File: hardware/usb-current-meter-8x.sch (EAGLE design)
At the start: 154 parts, among them IC10 OPA2234U, IC12 LTC485S, IC2 OPA2234U, IC3 MEGA48/88/168-AU, IC4 OPA2234U, IC5 OPA2234U, IC6 OPA2234U, IC7 OPA2234U, IC8 OPA2234U, IC9 OPA2234U, U3 RJ45-8PTH, X1 MC2, X2 MC2, X3 MC2, X4 MC2, X5 MC2, X6 MC2, X7 MC2, X8 MC2

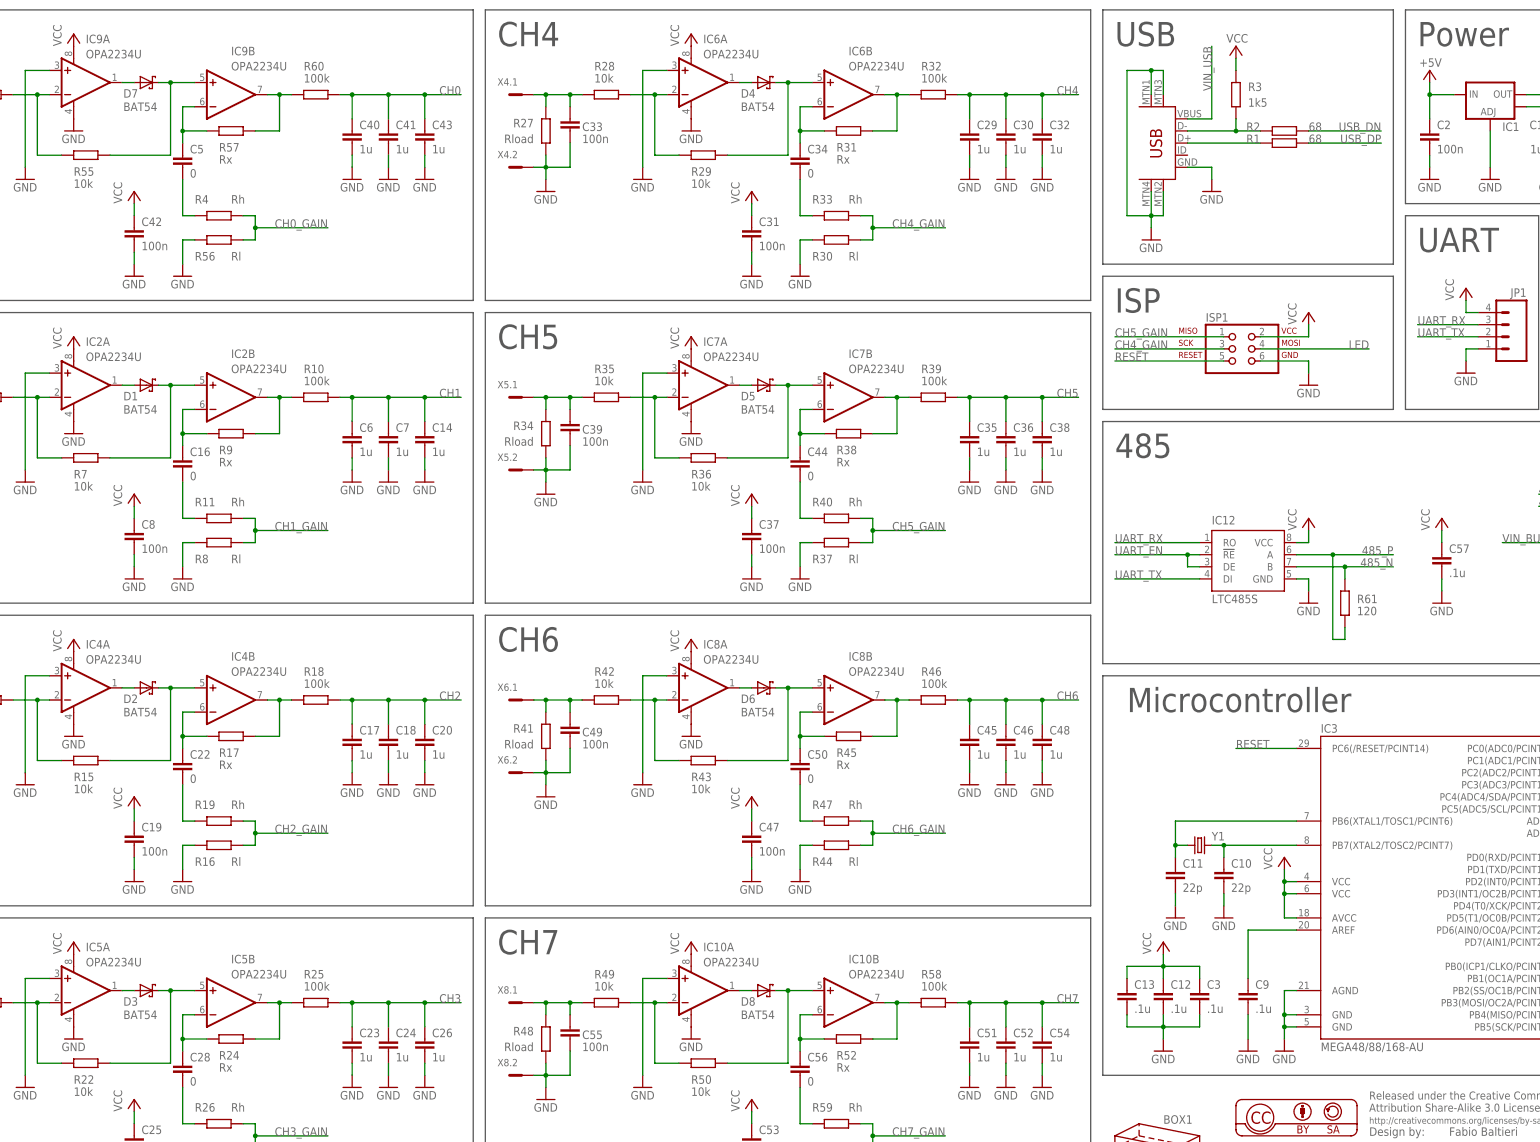
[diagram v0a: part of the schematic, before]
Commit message: hw: 8x: add part numbers
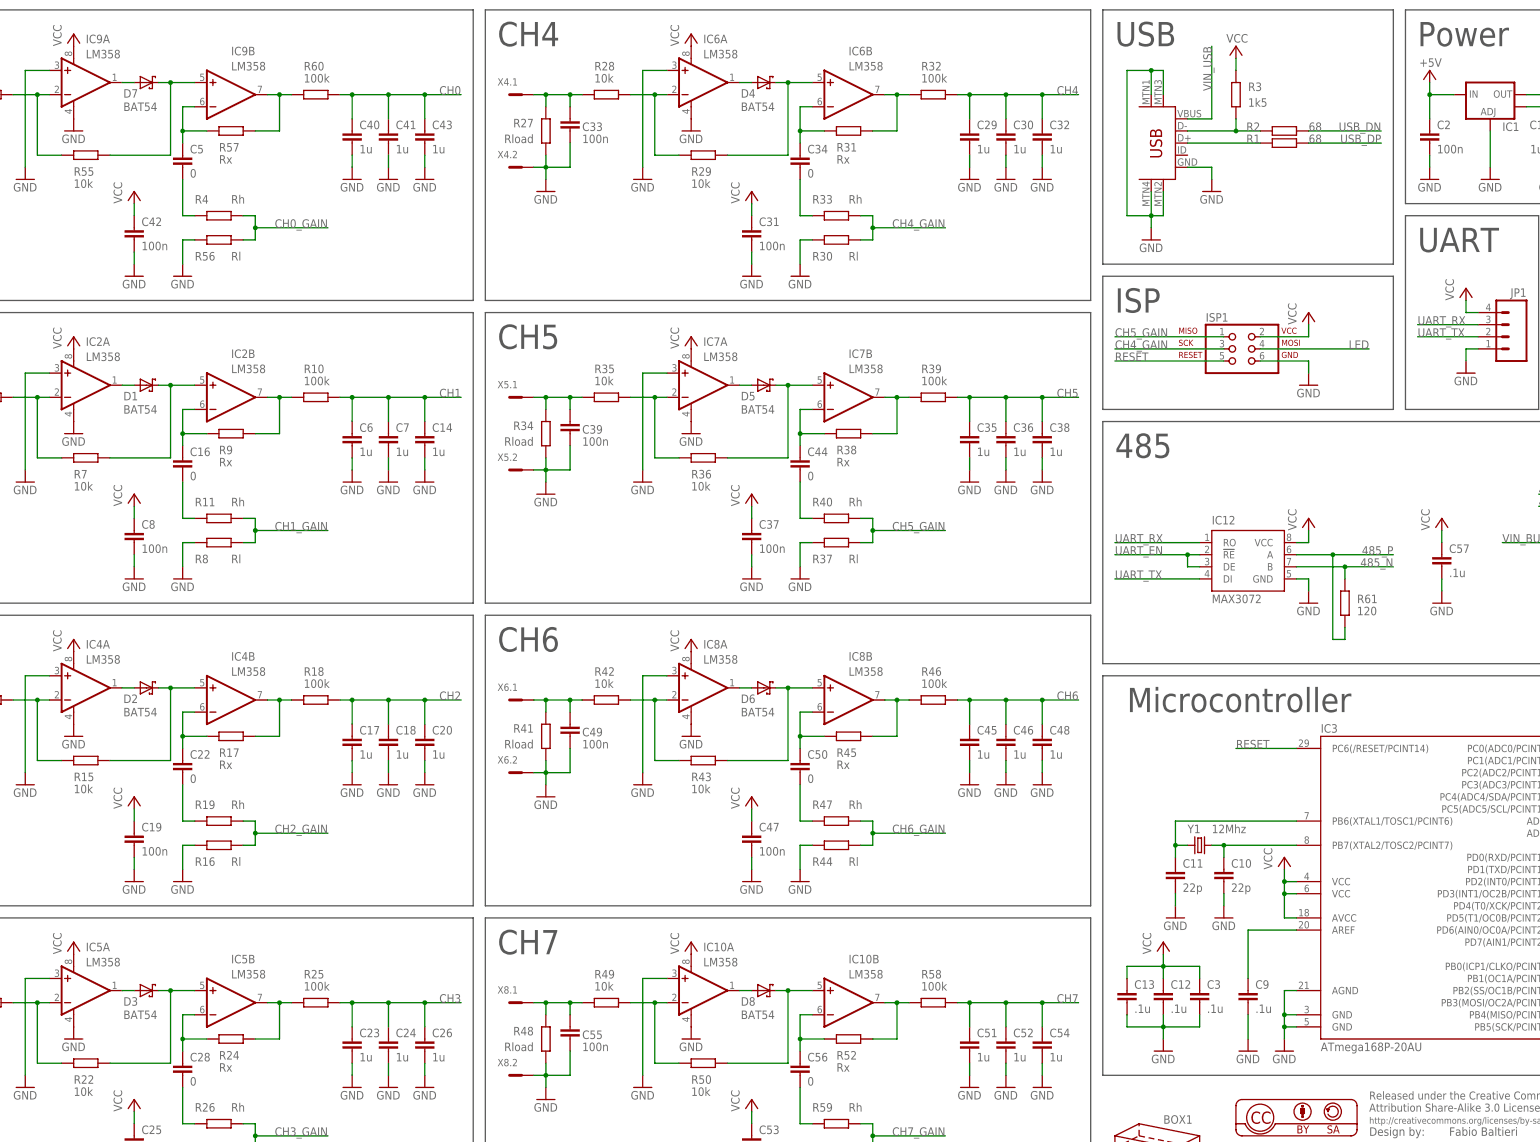
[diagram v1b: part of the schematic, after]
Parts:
- IC10, IC2, IC4, IC5, IC6, IC7, IC8, IC9: value OPA2234U -> LM358
- IC12: value LTC485S -> MAX3072
- IC3: value MEGA48/88/168-AU -> ATmega168P-20AU
- Y1: value (none) -> 12Mhz
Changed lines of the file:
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@@
 <part name="U$1" library="SparkFun" deviceset="USB-MINIB" device="-5PIN"/>
 <part name="GND11" library="supply1" deviceset="GND" device=""/>
-<part name="Y1" library="SparkFun" deviceset="CRYSTAL" device="HC49UV"/>
+<part name="Y1" library="SparkFun" deviceset="CRYSTAL" device="HC49UV" value="12Mhz"/>
 <part name="P+10" library="supply1" deviceset="VCC" device=""/>
 <part name="C9" library="rcl" deviceset="C-EU" device="C0805" value=".1u"/>
@@
 <part name="C12" library="rcl" deviceset="C-EU" device="C0805" value=".1u"/>
 <part name="C13" library="rcl" deviceset="C-EU" device="C0805" value=".1u"/>
-<part name="IC3" library="avr-5" deviceset="MEGA48/88/168" device="-AU"/>
+<part name="IC3" library="avr-5" deviceset="MEGA48/88/168" device="-AU" value="ATmega168P-20AU"/>
 <part name="FRAME1" library="frames" deviceset="DINA3_L" device=""/>
-<part name="IC9" library="burr-brown" deviceset="OPA2234" device="U"/>
+<part name="IC9" library="burr-brown" deviceset="OPA2234" device="U" value="LM358"/>
 <part name="X7" library="con-phoenix-381_l" deviceset="MC2" device=""/>
 <part name="D7" library="diode" deviceset="BAT54" device=""/>
@@
 <part name="P+6" library="supply1" deviceset="VCC" device=""/>
 <part name="GND7" library="supply1" deviceset="GND" device=""/>
-<part name="IC2" library="burr-brown" deviceset="OPA2234" device="U"/>
+<part name="IC2" library="burr-brown" deviceset="OPA2234" device="U" value="LM358"/>
 <part name="X1" library="con-phoenix-381_l" deviceset="MC2" device=""/>
 <part name="D1" library="diode" deviceset="BAT54" device=""/>
@@
 <part name="R11" library="rcl" deviceset="R-EU_" device="R0603" value="Rh"/>
 <part name="C16" library="rcl" deviceset="C-EU" device="C0805" value="0"/>
-<part name="IC4" library="burr-brown" deviceset="OPA2234" device="U"/>
+<part name="IC4" library="burr-brown" deviceset="OPA2234" device="U" value="LM358"/>
 <part name="X2" library="con-phoenix-381_l" deviceset="MC2" device=""/>
 <part name="D2" library="diode" deviceset="BAT54" device=""/>
@@
 <part name="R19" library="rcl" deviceset="R-EU_" device="R0603" value="Rh"/>
 <part name="C22" library="rcl" deviceset="C-EU" device="C0805" value="0"/>
-<part name="IC5" library="burr-brown" deviceset="OPA2234" device="U"/>
+<part name="IC5" library="burr-brown" deviceset="OPA2234" device="U" value="LM358"/>
 <part name="X3" library="con-phoenix-381_l" deviceset="MC2" device=""/>
 <part name="D3" library="diode" deviceset="BAT54" device=""/>
@@
 <part name="R26" library="rcl" deviceset="R-EU_" device="R0603" value="Rh"/>
 <part name="C28" library="rcl" deviceset="C-EU" device="C0805" value="0"/>
-<part name="IC6" library="burr-brown" deviceset="OPA2234" device="U"/>
+<part name="IC6" library="burr-brown" deviceset="OPA2234" device="U" value="LM358"/>
 <part name="X4" library="con-phoenix-381_l" deviceset="MC2" device=""/>
 <part name="D4" library="diode" deviceset="BAT54" device=""/>
@@
 <part name="R33" library="rcl" deviceset="R-EU_" device="R0603" value="Rh"/>
 <part name="C34" library="rcl" deviceset="C-EU" device="C0805" value="0"/>
-<part name="IC7" library="burr-brown" deviceset="OPA2234" device="U"/>
+<part name="IC7" library="burr-brown" deviceset="OPA2234" device="U" value="LM358"/>
 <part name="X5" library="con-phoenix-381_l" deviceset="MC2" device=""/>
 <part name="D5" library="diode" deviceset="BAT54" device=""/>
@@
 <part name="R40" library="rcl" deviceset="R-EU_" device="R0603" value="Rh"/>
 <part name="C44" library="rcl" deviceset="C-EU" device="C0805" value="0"/>
-<part name="IC8" library="burr-brown" deviceset="OPA2234" device="U"/>
+<part name="IC8" library="burr-brown" deviceset="OPA2234" device="U" value="LM358"/>
 <part name="X6" library="con-phoenix-381_l" deviceset="MC2" device=""/>
 <part name="D6" library="diode" deviceset="BAT54" device=""/>
@@
 <part name="R47" library="rcl" deviceset="R-EU_" device="R0603" value="Rh"/>
 <part name="C50" library="rcl" deviceset="C-EU" device="C0805" value="0"/>
-<part name="IC10" library="burr-brown" deviceset="OPA2234" device="U"/>
+<part name="IC10" library="burr-brown" deviceset="OPA2234" device="U" value="LM358"/>
 <part name="X8" library="con-phoenix-381_l" deviceset="MC2" device=""/>
 <part name="D8" library="diode" deviceset="BAT54" device=""/>
@@
 <part name="R59" library="rcl" deviceset="R-EU_" device="R0603" value="Rh"/>
 <part name="C56" library="rcl" deviceset="C-EU" device="C0805" value="0"/>
-<part name="IC12" library="linear-technology" deviceset="LTC485" device="S"/>
+<part name="IC12" library="linear-technology" deviceset="LTC485" device="S" value="MAX3072"/>
 <part name="C57" library="rcl" deviceset="C-EU" device="C0805" value=".1u"/>
 <part name="GND79" library="supply1" deviceset="GND" device=""/>
@@
 <instance part="U$1" gate="G$1" x="276.86" y="228.6" rot="MR0"/>
 <instance part="GND11" gate="1" x="271.78" y="213.36"/>
-<instance part="Y1" gate="G$1" x="281.94" y="86.36"/>
+<instance part="Y1" gate="G$1" x="281.94" y="86.36" smashed="yes">
+<attribute name="NAME" x="279.4" y="88.9" size="1.778" layer="95"/>
+<attribute name="VALUE" x="284.48" y="88.9" size="1.778" layer="96"/>
+</instance>
 <instance part="P+10" gate="VCC" x="299.72" y="83.82"/>
 <instance part="C9" gate="G$1" x="292.1" y="55.88"/>

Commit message: hw: 8x: clean up schematics, add calcs
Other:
- note added: "Bidge"
- note added: "Gain = 3.3 / .12 + 1 = 28.5"
- note added: "Gain = 3.3 / 2.22 + 1 = 2.42"
- note added: "Ipk = Irms * sqrt(2) = 40.0 A"
- note added: "Irms = Pmax / 230 = 28.2 A"
- note added: "Pmax = 6500 W"
- note added: "Psatuation = 592 W"
- note added: "Rh = 120 Ohm, Rl = 2200 Ohm, Rx = 3300 Ohm"
- note added: "Vavg = Vpk * 2 / pi = .424 V"
- note added: "Vavg_post = Vavg * Gain = 1.026 V"
- note added: "Vavg_post = Vavg * Gain = 12.074 V"
- note added: "Vpk = .333 / 20 * Ipk = .665 V"
- note added: "Vpk_post = Vpk * Gain = 1.612 V"
- note added: "Vpk_post = Vpk * Gain = 18.965 V"
- moved on the sheet: D9
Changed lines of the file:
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@@
 <wire x1="386.08" y1="124.46" x2="386.08" y2="175.26" width="0.1524" layer="97"/>
 <text x="264.16" y="167.64" size="5.08" layer="97">485</text>
+<wire x1="355.6" y1="218.44" x2="355.6" y2="177.8" width="0.1524" layer="97"/>
+<wire x1="383.54" y1="218.44" x2="383.54" y2="177.8" width="0.1524" layer="97"/>
+<wire x1="355.6" y1="218.44" x2="383.54" y2="218.44" width="0.1524" layer="97"/>
+<wire x1="355.6" y1="177.8" x2="383.54" y2="177.8" width="0.1524" layer="97"/>
+<text x="358.14" y="210.82" size="5.08" layer="97">Bidge</text>
+<text x="25.4" y="297.18" size="1.778" layer="97">Pmax = 6500 W</text>
+<text x="25.4" y="294.64" size="1.778" layer="97">Irms = Pmax / 230 = 28.2 A</text>
+<text x="25.4" y="292.1" size="1.778" layer="97">Ipk = Irms * sqrt(2) = 40.0 A</text>
+<text x="25.4" y="289.56" size="1.778" layer="97">Vpk = .333 / 20 * Ipk = .665 V</text>
+<text x="25.4" y="287.02" size="1.778" layer="97">Vavg = Vpk * 2 / pi = .424 V</text>
+<text x="5.08" y="276.86" size="1.778" layer="97">Gain = 3.3 / .12 + 1 = 28.5</text>
+<text x="5.08" y="274.32" size="1.778" layer="97">Vpk_post = Vpk * Gain = 18.965 V</text>
+<text x="5.08" y="271.78" size="1.778" layer="97">Vavg_post = Vavg * Gain = 12.074 V</text>
+<wire x1="2.54" y1="266.7" x2="2.54" y2="299.72" width="0.1524" layer="97"/>
+<text x="25.4" y="281.94" size="1.778" layer="97">Rh = 120 Ohm, Rl = 2200 Ohm, Rx = 3300 Ohm</text>
+<text x="60.96" y="276.86" size="1.778" layer="97">Gain = 3.3 / 2.22 + 1 = 2.42</text>
+<text x="60.96" y="274.32" size="1.778" layer="97">Vpk_post = Vpk * Gain = 1.612 V</text>
+<text x="60.96" y="271.78" size="1.778" layer="97">Vavg_post = Vavg * Gain = 1.026 V</text>
+<wire x1="114.3" y1="266.7" x2="114.3" y2="299.72" width="0.1524" layer="97"/>
+<wire x1="2.54" y1="299.72" x2="114.3" y2="299.72" width="0.1524" layer="97"/>
+<wire x1="114.3" y1="266.7" x2="2.54" y2="266.7" width="0.1524" layer="97"/>
+<text x="5.08" y="269.24" size="1.778" layer="97">Psatuation = 592 W</text>
 </plain>
 <instances>
@@
 <instance part="GND82" gate="1" x="332.74" y="137.16"/>
 <instance part="BOX1" gate="G$1" x="269.24" y="27.94"/>
-<instance part="D9" gate="G$1" x="368.3" y="198.12" rot="R270"/>
-<instance part="P+25" gate="1" x="375.92" y="205.74" smashed="yes">
-<attribute name="VALUE" x="373.38" y="203.2" size="1.778" layer="96" rot="R90"/>
+<instance part="D9" gate="G$1" x="370.84" y="190.5" rot="R270"/>
+<instance part="P+25" gate="1" x="378.46" y="198.12" smashed="yes">
+<attribute name="VALUE" x="375.92" y="195.58" size="1.778" layer="96" rot="R90"/>
 </instance>
 </instances>
@@
 <pinref part="D9" gate="G$1" pin="CC"/>
 <pinref part="P+25" gate="1" pin="+5V"/>
-<wire x1="370.84" y1="198.12" x2="375.92" y2="198.12" width="0.1524" layer="91"/>
-<wire x1="375.92" y1="198.12" x2="375.92" y2="203.2" width="0.1524" layer="91"/>
+<wire x1="373.38" y1="190.5" x2="378.46" y2="190.5" width="0.1524" layer="91"/>
+<wire x1="378.46" y1="190.5" x2="378.46" y2="195.58" width="0.1524" layer="91"/>
 </segment>
 </net>
@@
 <segment>
 <pinref part="D9" gate="G$1" pin="A1"/>
-<wire x1="368.3" y1="203.2" x2="368.3" y2="205.74" width="0.1524" layer="91"/>
-<wire x1="368.3" y1="205.74" x2="358.14" y2="205.74" width="0.1524" layer="91"/>
-<label x="358.14" y="205.74" size="1.778" layer="95"/>
+<wire x1="370.84" y1="195.58" x2="370.84" y2="198.12" width="0.1524" layer="91"/>
+<wire x1="370.84" y1="198.12" x2="360.68" y2="198.12" width="0.1524" layer="91"/>
+<label x="360.68" y="198.12" size="1.778" layer="95"/>
 </segment>
 </net>
@@
 <segment>
 <pinref part="D9" gate="G$1" pin="A2"/>
-<wire x1="368.3" y1="193.04" x2="368.3" y2="190.5" width="0.1524" layer="91"/>
-<wire x1="368.3" y1="190.5" x2="358.14" y2="190.5" width="0.1524" layer="91"/>
-<label x="358.14" y="190.5" size="1.778" layer="95" rot="MR180"/>
-</segment>
-</net>
+<wire x1="370.84" y1="185.42" x2="370.84" y2="182.88" width="0.1524" layer="91"/>
+<wire x1="370.84" y1="182.88" x2="360.68" y2="182.88" width="0.1524" layer="91"/>
+<label x="360.68" y="182.88" size="1.778" layer="95" rot="MR180"/>
+</segment>
+</net>
